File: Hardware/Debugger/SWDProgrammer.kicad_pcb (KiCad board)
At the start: 4 copper layers, 24.5 x 31 mm, 40 parts, among them J1 USB_C_Receptacle_USB2.0, J2 USB_C_Receptacle_USB2.0, U1 AP2112K-3.3, U2 STM32F103C8Tx, Y1 32.768KHZ, Y2 8Mhz

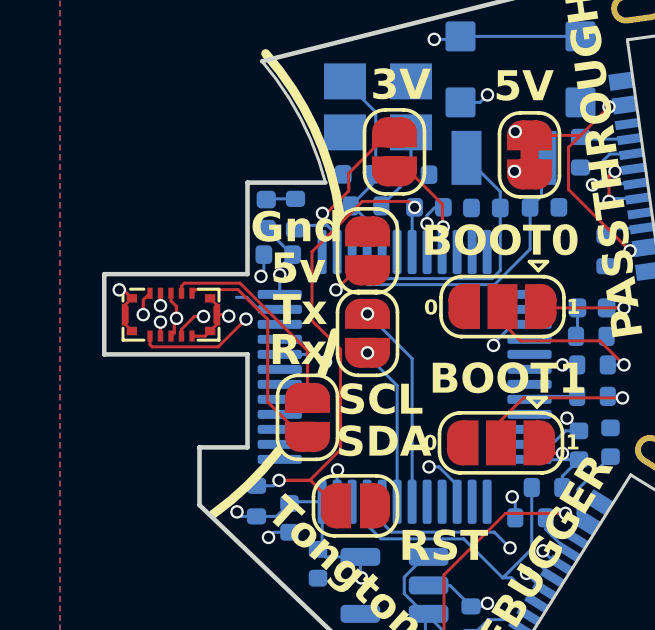
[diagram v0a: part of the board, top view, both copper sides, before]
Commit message: fixed debugger datapin board, connected dir and out of as5600 to mcu
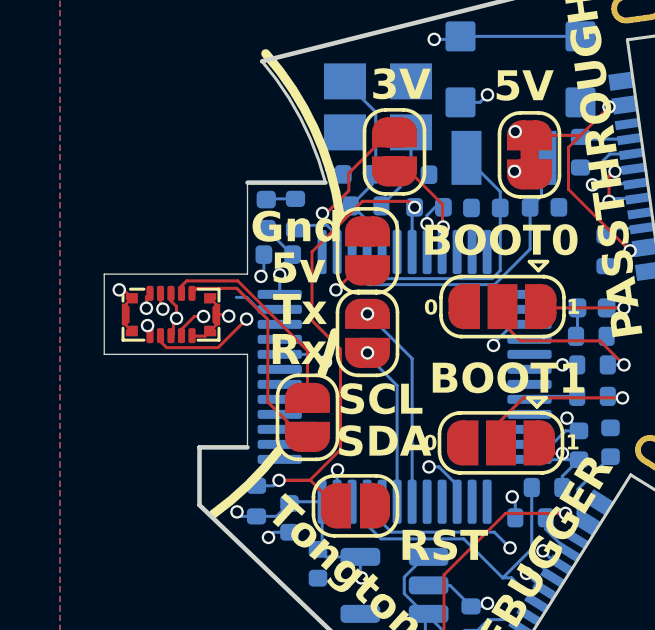
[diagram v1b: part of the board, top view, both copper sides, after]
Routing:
- net D+: track 22.1 -> 21.6 mm
